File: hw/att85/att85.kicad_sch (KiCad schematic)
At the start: 37 parts, among them J101 Barrel_Jack_Switch, J102 Screw_Terminal_01x03, J104 Conn_01x02, Q101 BC817, SW101 SW_Push, SW102 SW_Push, SW103 SW_Push, SW104 SW_Push, SW105 SW_Push, SW106 SW_Push, U102 MT3608-MODULE, U103 VS1838B

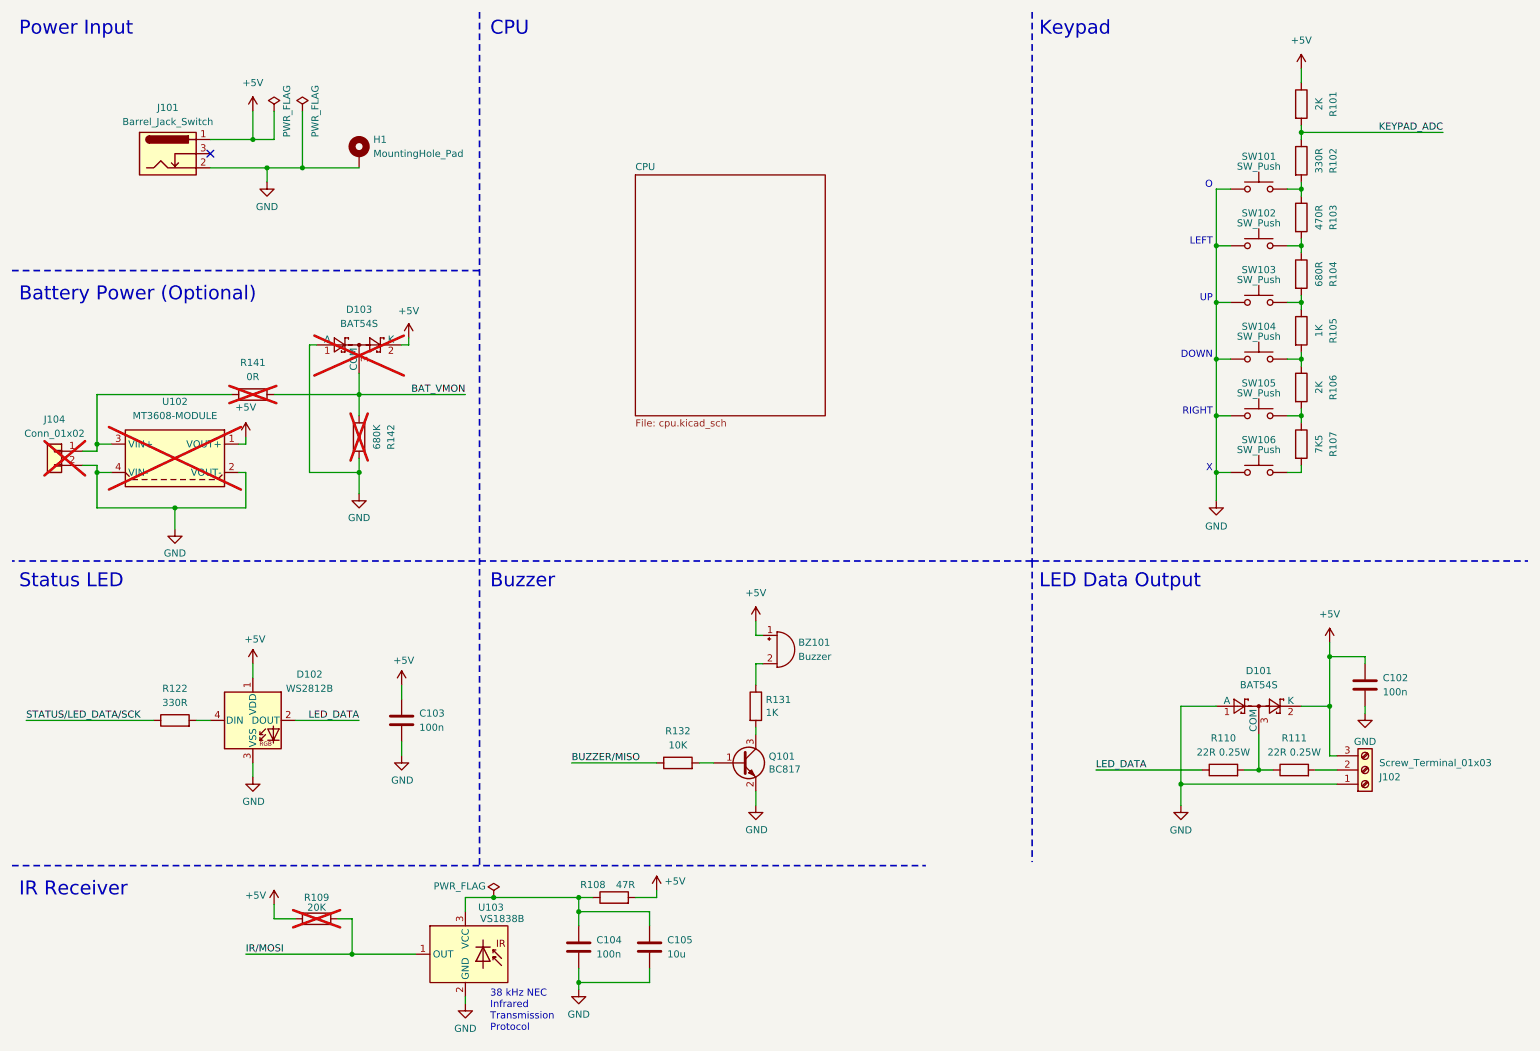
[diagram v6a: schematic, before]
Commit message: chore(hw): organize schematics into sheets, sync with layout
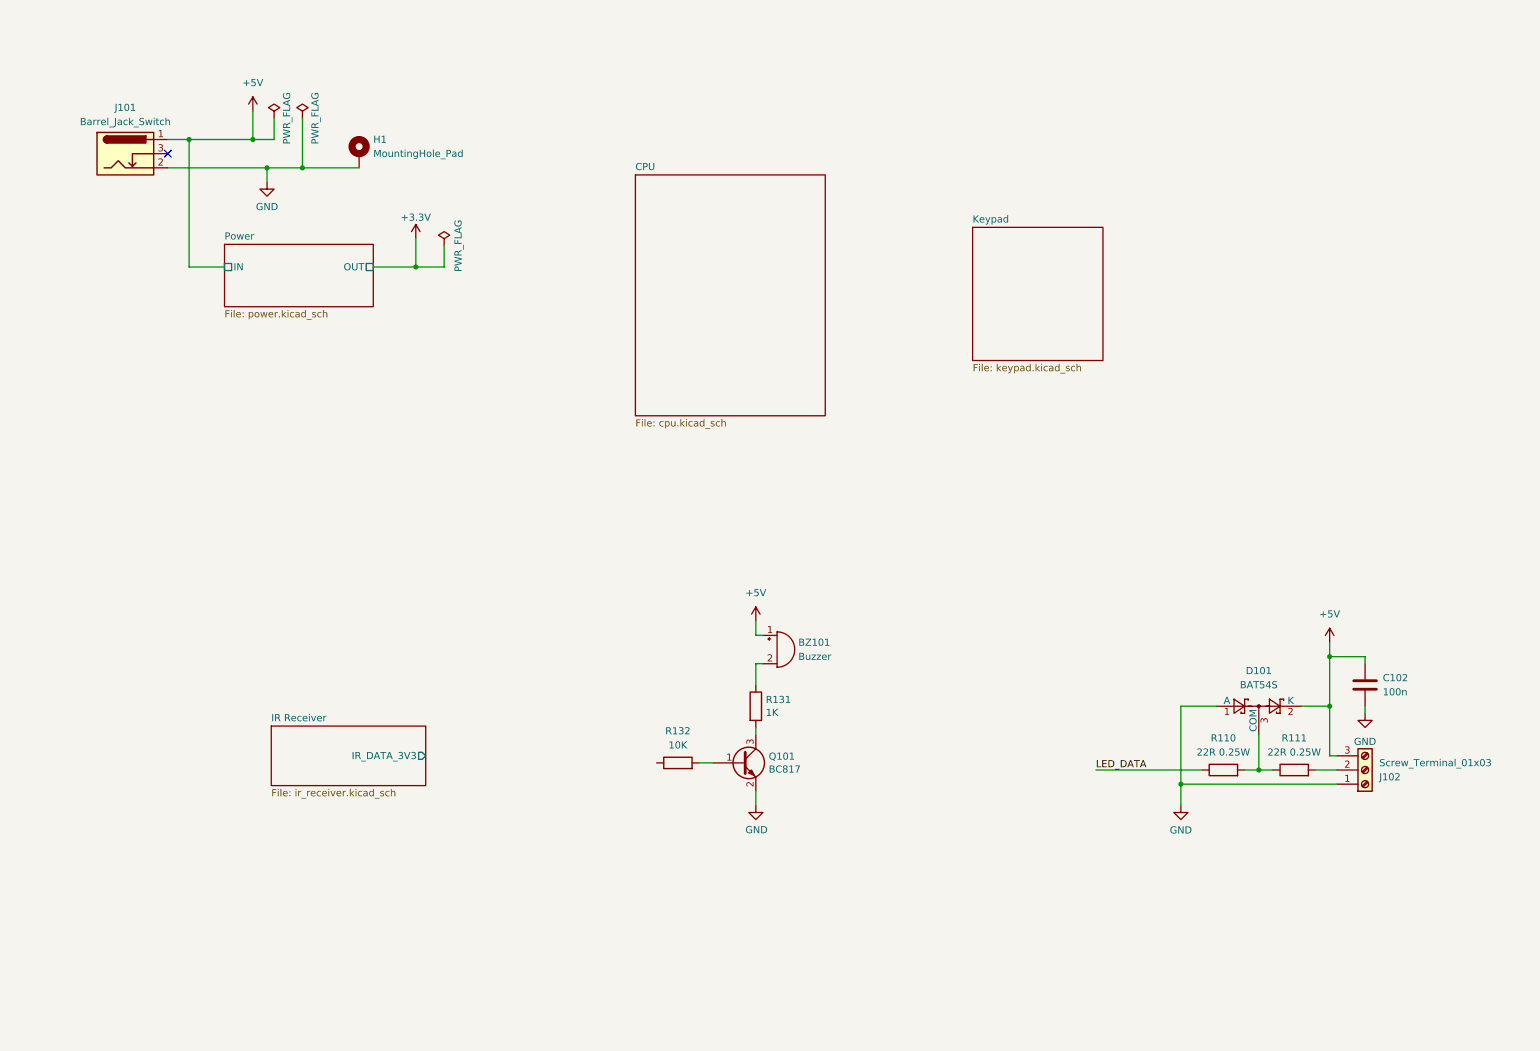
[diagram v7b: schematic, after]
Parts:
- removed C103, C104: 100n, Capacitor_SMD:C_0805_2012Metric_Pad1.18x1.45mm_HandSolder, symbol Device:C
- removed C105: 10u, Capacitor_SMD:C_1206_3216Metric_Pad1.33x1.80mm_HandSolder, symbol Device:C
- removed D102: WS2812B, LED_SMD:LED_WS2812B_PLCC4_5.0x5.0mm_P3.2mm, symbol LED:WS2812B
- removed D103: BAT54S, Package_TO_SOT_SMD:SOT-23, symbol Diode:BAT54S
- removed J104: Conn_01x02, Connector_JST:JST_PH_B2B-PH-K_1x02_P2.00mm_Vertical, symbol Connector_Generic:Conn_01x02
- removed R101, R106: 2K, Resistor_SMD:R_0805_2012Metric_Pad1.20x1.40mm_HandSolder, symbol Device:R
- removed R102, R122: 330R, Resistor_SMD:R_0805_2012Metric_Pad1.20x1.40mm_HandSolder, symbol Device:R
- removed R103: 470R, Resistor_SMD:R_0805_2012Metric_Pad1.20x1.40mm_HandSolder, symbol Device:R
- removed R104: 680R, Resistor_SMD:R_0805_2012Metric_Pad1.20x1.40mm_HandSolder, symbol Device:R
- removed R105: 1K, Resistor_SMD:R_0805_2012Metric_Pad1.20x1.40mm_HandSolder, symbol Device:R
- removed R107: 7K5, Resistor_SMD:R_0805_2012Metric_Pad1.20x1.40mm_HandSolder, symbol Device:R
- removed R108: 47R, Resistor_SMD:R_0805_2012Metric_Pad1.20x1.40mm_HandSolder, symbol Device:R
- removed R109: 20K, Resistor_SMD:R_0805_2012Metric_Pad1.20x1.40mm_HandSolder, symbol Device:R
- removed R141: 0R, project-specific:R_0805_2012Metric_Pad1.20x1.40mm_HandSolder_Jumper, symbol Device:R
- removed R142: 680K, Resistor_SMD:R_0805_2012Metric_Pad1.20x1.40mm_HandSolder, symbol Device:R
- removed SW101, SW102, SW103, SW104, SW105, SW106: SW_Push, Button_Switch_THT:SW_PUSH_6mm, symbol Switch:SW_Push
- removed U102: MT3608-MODULE, project-specific:mt3608-module, symbol project-specific:mt3608-module
- removed U103: VS1838B, Connector_PinSocket_2.54mm:PinSocket_1x03_P2.54mm_Vertical, symbol project-specific:IR_Receiver
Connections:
- net BUZZER/MISO: no longer names the net of R132.1
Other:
- added sheet IR Receiver (ir_receiver.kicad_sch)
- added sheet Keypad (keypad.kicad_sch)
- added sheet Power (power.kicad_sch)
- note removed: "38 kHz NEC Infrared Transmission Protocol"
- note removed: "Battery Power (Optional)"
- note removed: "Buzzer"
- note removed: "CPU"
- note removed: "DOWN"
- note removed: "IR Receiver"
- note removed: "Keypad"
- note removed: "LED Data Output"
- note removed: "LEFT"
- note removed: "O"
- note removed: "Power Input"
- note removed: "RIGHT"
- note removed: "Status LED"
- note removed: "UP"
- note removed: "X"
- moved on the sheet: J101

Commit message: chore(hw): wired basic connections, organized main sheet
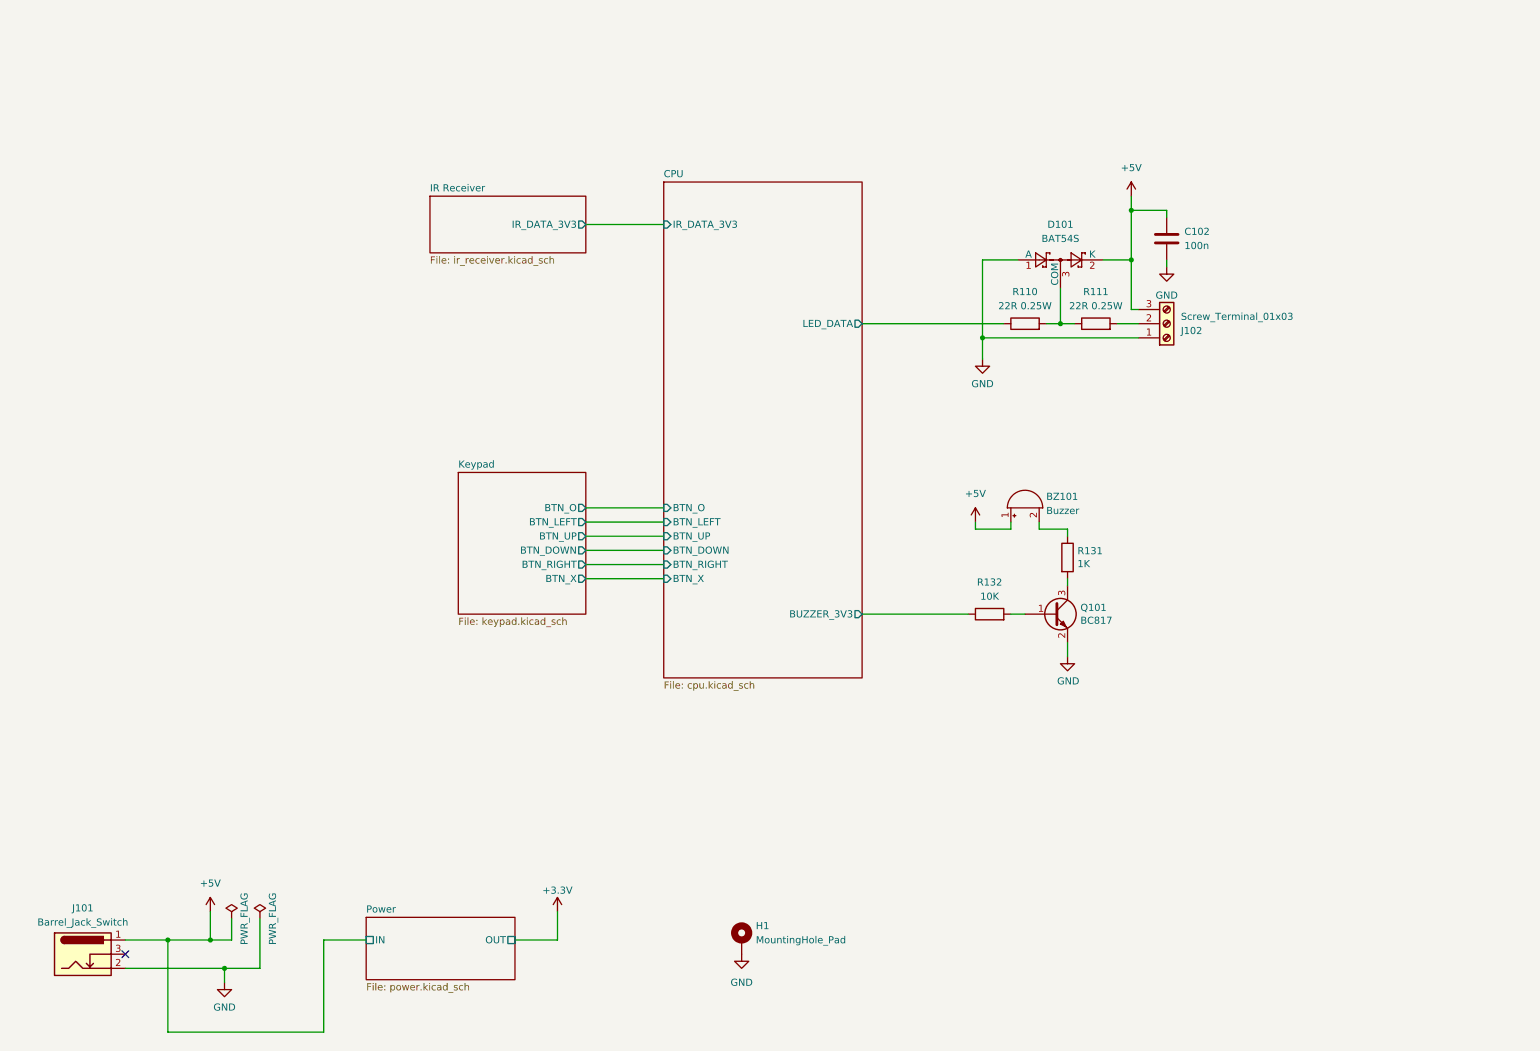
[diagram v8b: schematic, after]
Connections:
- net CPU/BUZZER_3V3: now reaches R132.1
- net LED_DATA renamed CPU/LED_DATA
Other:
- sheet CPU ports: added BTN_DOWN, BTN_LEFT, BTN_O, BTN_RIGHT, BTN_UP, BTN_X, BUZZER_3V3, IR_DATA_3V3, LED_DATA; removed none
- sheet Keypad ports: added BTN_DOWN, BTN_LEFT, BTN_O, BTN_RIGHT, BTN_UP, BTN_X; removed none
- moved on the sheet: BZ101, C102, D101, H1, J101, J102, Q101, R110, R111, R131, R132
